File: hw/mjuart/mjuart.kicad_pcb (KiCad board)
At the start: 4 copper layers, 24.5 x 14 mm, 16 parts, among them J1 S4B-ZR-SM4A-TFLFSN, J2 USB4110-GF-A, J3 Conn_01x04_Pin, J4 Conn_01x04_Pin, U1 FT231XQ

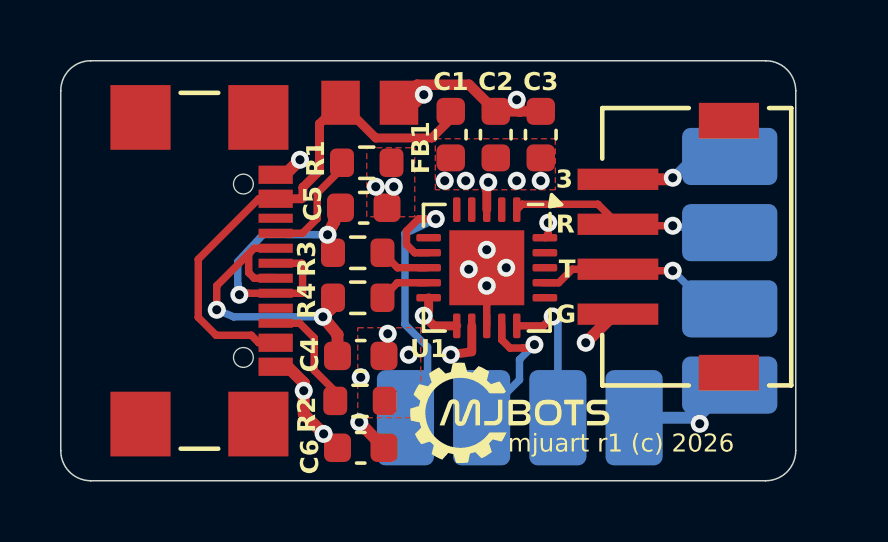
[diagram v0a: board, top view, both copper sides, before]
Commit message: mjuart: Fix ZH4 pinout to match moteus-r4
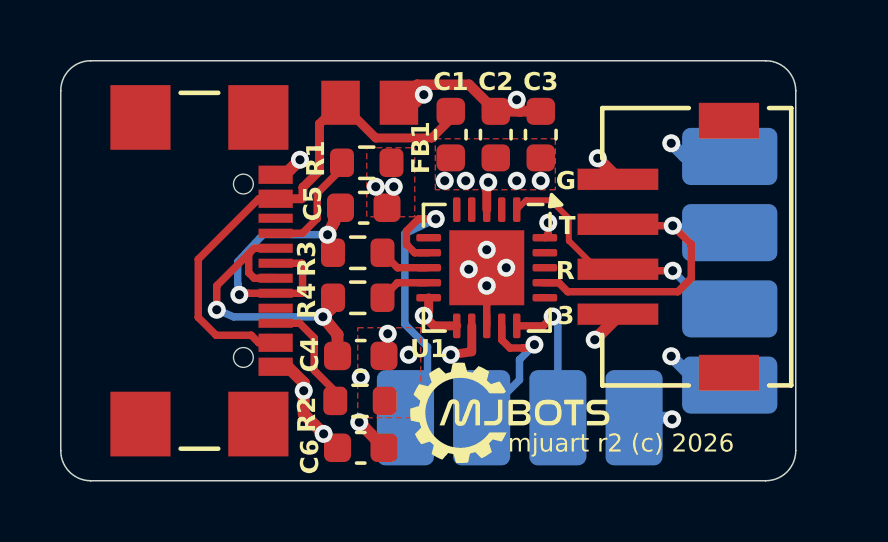
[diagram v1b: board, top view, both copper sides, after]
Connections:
- J1 pad 1: GND -> +3V
- J1 pad 4: +3V -> GND
- J3 pad 1: GND -> +3V
- J3 pad 4: +3V -> GND
- U1 pad 1: Net-(J3-Pin_3) -> Net-(J3-Pin_2)
- U1 pad 17: Net-(J3-Pin_2) -> Net-(J3-Pin_3)
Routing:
- net Net-(J3-Pin_3): track 7.41 -> 10.9 mm
- net Net-(J3-Pin_2): track 6.88 -> 9.01 mm
- net +3V: track 7.68 -> 7.36 mm, vias 4 -> 5
- net GND: track 13.7 -> 13.6 mm, vias 19 -> 20
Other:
- board text added: "mjuart r2 (c) 2026"
- board text removed: "GND"
- board text removed: "mjuart r1 (c) 2026"
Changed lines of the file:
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@@
 			(size 0.7112 2.6924)
 			(layers "F.Cu" "F.Mask" "F.Paste")
-			(net 1 "GND")
+			(net 2 "+3V")
 			(pinfunction "1")
 			(pintype "unspecified")
@@
 			(size 0.7112 2.6924)
 			(layers "F.Cu" "F.Mask" "F.Paste")
-			(net 2 "+3V")
+			(net 1 "GND")
 			(pinfunction "4")
 			(pintype "unspecified")
@@
 			(layers "F.Cu" "F.Mask" "F.Paste")
 			(roundrect_rratio 0.25)
-			(net 20 "Net-(J3-Pin_3)")
+			(net 21 "Net-(J3-Pin_2)")
 			(pinfunction "RXD")
 			(pintype "input")
@@
 			(layers "F.Cu" "F.Mask" "F.Paste")
 			(roundrect_rratio 0.25)
-			(net 21 "Net-(J3-Pin_2)")
+			(net 20 "Net-(J3-Pin_3)")
 			(pinfunction "TXD")
 			(pintype "output")
@@
 			(layers "B.Cu" "B.Mask")
 			(roundrect_rratio 0.15)
-			(net 1 "GND")
+			(net 2 "+3V")
 			(pinfunction "Pin_1")
 			(pintype "passive")
@@
 			(layers "B.Cu" "B.Mask")
 			(roundrect_rratio 0.15)
-			(net 2 "+3V")
+			(net 1 "GND")
 			(pinfunction "Pin_4")
 			(pintype "passive")
@@
 	)
 	(gr_text "T"
-		(at 156.6 107.3 0)
+		(at 156.6 105.85 0)
 		(layer "F.SilkS")
 		(effects
@@
 	)
 	(gr_text "G"
-		(at 156.5 108.8 0)
+		(at 156.5 104.35 0)
 		(layer "F.SilkS")
 		(effects
@@
 	)
 	(gr_text "3"
-		(at 156.5 104.3 0)
+		(at 156.55 108.85 0)
 		(layer "F.SilkS")
 		(effects
@@
 		)
 	)
-	(gr_text "mjuart r1 (c) 2026"
+	(gr_text "mjuart r2 (c) 2026"
 		(at 154.9 113.1 0)
 		(layer "F.SilkS")
@@
 	)
 	(gr_text "R"
-		(at 156.5 105.8 0)
+		(at 156.5 107.35 0)
 		(layer "F.SilkS")
 		(effects
@@
 	)
 	(gr_text "3V"
-		(at 160.2 103.8 0)
+		(at 163.35 113.05 0)
 		(layer "B.SilkS")
 		(effects
@@
 	)
 	(gr_text "TX"
-		(at 160.2 108.9 0)
+		(at 160.1 106.45 0)
 		(layer "B.SilkS")
 		(effects
@@
 	)
 	(gr_text "RX"
-		(at 160.2 106.3 0)
+		(at 160.15 108.8 0)
 		(layer "B.SilkS")
 		(effects
@@
 		)
 	)
-	(gr_text "GND"
-		(at 163.4 113.7 0)
+	(gr_text "G"
+		(at 158.1 110.4 270)
+		(layer "B.SilkS")
+		(effects
+			(font
+				(size 1 1)
+				(thickness 0.15)
+			)
+			(justify left bottom mirror)
+		)
+	)
+	(gr_text "G"
+		(at 160.2 103.95 0)
 		(layer "B.SilkS")
 		(effects
@@
 	)
 	(segment
+		(start 158.572601 103.922601)
+		(end 157.9 103.25)
+		(width 0.4)
+		(layer "F.Cu")
+		(net 1)
+	)
+	(segment
 		(start 147.1628 103.799999)
 		(end 147.336582 103.799999)
@@
 	)
 	(segment
-		(start 158.65 108.45)
-		(end 158.45 108.45)
+		(start 158.572601 103.9521)
+		(end 158.572601 103.922601)
 		(width 0.4)
 		(layer "F.Cu")
@@
 	)
 	(segment
-		(start 158.45 108.45)
-		(end 157.5 109.4)
-		(width 0.4)
-		(layer "F.Cu")
-		(net 1)
-	)
-	(segment
 		(start 149.225 112.9)
 		(end 148.1 111.775)
@@
 	)
 	(via
-		(at 161.3 112.1)
-		(size 0.6)
-		(drill 0.3)
-		(layers "F.Cu" "B.Cu")
-		(net 1)
-	)
-	(via
 		(at 154.2 106.3)
 		(size 0.6)
@@
 	)
 	(via
-		(at 157.5 109.4)
+		(at 152.8 104)
 		(size 0.6)
 		(drill 0.3)
 		(layers "F.Cu" "B.Cu")
+		(free yes)
 		(net 1)
 	)
 	(via
-		(at 152.8 104)
+		(at 160.379486 111.951691)
 		(size 0.6)
 		(drill 0.3)
 		(layers "F.Cu" "B.Cu")
-		(free yes)
 		(net 1)
 	)
@@
 	)
 	(via
+		(at 160.35 102.75)
+		(size 0.6)
+		(drill 0.3)
+		(layers "F.Cu" "B.Cu")
+		(net 1)
+	)
+	(via
 		(at 154.85 106.9)
 		(size 0.6)
@@
 	)
 	(via
+		(at 157.9 103.25)
+		(size 0.6)
+		(drill 0.3)
+		(layers "F.Cu" "B.Cu")
+		(net 1)
+	)
+	(via
 		(at 150.9 109.1)
 		(size 0.6)
@@
 	)
 	(segment
+		(start 162.3 103)
+		(end 161.3 103)
+		(width 0.3)
+		(layer "B.Cu")
+		(net 1)
+	)
+	(segment
 		(start 159.11 111.9)
-		(end 161.1 111.9)
+		(end 160.327795 111.9)
 		(width 0.4)
 		(layer "B.Cu")
@@
 	)
 	(segment
-		(start 161.3 112.1)
-		(end 161.3 111.81)
+		(start 160.327795 111.9)
+		(end 160.379486 111.951691)
 		(width 0.4)
 		(layer "B.Cu")
@@
 	)
 	(segment
-		(start 161.3 111.81)
-		(end 162.3 110.81)
+		(start 160.79 103.19)
+		(end 160.35 102.75)
 		(width 0.4)
 		(layer "B.Cu")
@@
 	)
 	(segment
-		(start 161.1 111.9)
-		(end 161.3 112.1)
+		(start 162.3 103.19)
+		(end 160.79 103.19)
 		(width 0.4)
 		(layer "B.Cu")
@@
 	)
 	(segment
+		(start 158.572601 108.527399)
+		(end 157.8 109.3)
+		(width 0.4)
+		(layer "F.Cu")
+		(net 2)
+	)
+	(segment
+		(start 158.572601 108.4479)
+		(end 158.572601 108.527399)
+		(width 0.4)
+		(layer "F.Cu")
+		(net 2)
+	)
+	(segment
 		(start 156.25 105.7875)
 		(end 156.1375 105.9)
@@
 	)
 	(segment
+		(start 158.65 108.45)
+		(end 158.45 108.45)
+		(width 0.4)
+		(layer "F.Cu")
+		(net 2)
+	)
+	(segment
 		(start 153.2 108.8375)
 		(end 152.4375 108.8375)
@@
 	)
 	(segment
-		(start 160.35 103.95)
-		(end 160.4 103.9)
-		(width 0.4)
-		(layer "F.Cu")
-		(net 2)
-	)
-	(segment
-		(start 158.65 103.95)
-		(end 160.35 103.95)
-		(width 0.4)
-		(layer "F.Cu")
-		(net 2)
-	)
-	(segment
 		(start 152.2625 107.9)
 		(end 152.2625 108.3375)
@@
 	)
 	(via
-		(at 160.4 103.9)
+		(at 160.35 109.85)
 		(size 0.6)
 		(drill 0.3)
@@
 		(net 2)
 	)
+	(via
+		(at 157.8 109.3)
+		(size 0.6)
+		(drill 0.3)
+		(layers "F.Cu" "B.Cu")
+		(net 2)
+	)
 	(segment
-		(start 162.3 103)
-		(end 161.3 103)
-		(width 0.3)
+		(start 162.3 110.81)
+		(end 161.31 110.81)
+		(width 0.4)
 		(layer "B.Cu")
 		(net 2)
 	)
 	(segment
-		(start 161.3 103)
-		(end 160.4 103.9)
-		(width 0.3)
+		(start 161.31 110.81)
+		(end 160.35 109.85)
+		(width 0.4)
 		(layer "B.Cu")
 		(net 2)
@@
 	)
 	(segment
-		(start 157.905901 104.784)
-		(end 158.572601 105.4507)
+		(start 160.571156 107.7)
+		(end 161.016 107.255156)
+		(width 0.25)
+		(layer "F.Cu")
+		(net 20)
+	)
+	(segment
+		(start 161.016 107.255156)
+		(end 161.016 106.116)
+		(width 0.25)
+		(layer "F.Cu")
+		(net 20)
+	)
+	(segment
+		(start 161.016 106.116)
+		(end 160.4 105.5)
 		(width 0.25)
 		(layer "F.Cu")
@@
 	)
 	(segment
-		(start 155.3785 104.784)
-		(end 157.905901 104.784)
+		(start 156.9 107.7)
+		(end 160.571156 107.7)
 		(width 0.25)
 		(layer "F.Cu")
@@
 	)
 	(segment
-		(start 155.2 104.9625)
-		(end 155.3785 104.784)
+		(start 156.6 107.4)
+		(end 156.9 107.7)
+		(width 0.25)
+		(layer "F.Cu")
+		(net 20)
+	)
+	(segment
+		(start 156.075 107.4)
+		(end 156.6 107.4)
 		(width 0.25)
 		(layer "F.Cu")
@@
 	)
 	(segment
+		(start 157.884701 106.9493)
+		(end 158.572601 106.9493)
+		(width 0.2)
+		(layer "F.Cu")
+		(net 21)
+	)
+	(segment
+		(start 156.935401 105.2496)
+		(end 156.935401 106)
+		(width 0.2)
+		(layer "F.Cu")
+		(net 21)
+	)
+	(segment
 		(start 158.7 107)
 		(end 158.65 106.95)
@@
 	)
 	(segment
-		(start 157.05 106.95)
-		(end 158.65 106.95)
-		(width 0.25)
+		(start 155.5125 104.65)
+		(end 156.335801 104.65)
+		(width 0.2)
 		(layer "F.Cu")
 		(net 21)
 	)
 	(segment
-		(start 156.6 107.4)
-		(end 157.05 106.95)
-		(width 0.25)
+		(start 155.2 104.9625)
+		(end 155.5125 104.65)
+		(width 0.2)
 		(layer "F.Cu")
 		(net 21)
 	)
 	(segment
-		(start 156.075 107.4)
-		(end 156.6 107.4)
-		(width 0.25)
+		(start 156.335801 104.65)
+		(end 156.935401 105.2496)
+		(width 0.2)
+		(layer "F.Cu")
+		(net 21)
+	)
+	(segment
+		(start 156.935401 106)
+		(end 157.884701 106.9493)
+		(width 0.2)
 		(layer "F.Cu")
 		(net 21)
